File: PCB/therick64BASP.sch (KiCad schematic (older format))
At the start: 172 parts, among them J1 TYPE-C-31-M12_13, J2 AVR-ISP-6_mod, K1 KEYSW, K10 KEYSW, K11 KEYSW, K12 KEYSW, K13 KEYSW, K14 KEYSW, K15 KEYSW, K16 KEYSW, K17 KEYSW, K18 KEYSW, K19 KEYSW, K2 KEYSW, K20 KEYSW, K21 KEYSW, K22 KEYSW, K23 KEYSW, K24 KEYSW, K25 KEYSW, K26 KEYSW, K27 KEYSW, K28 KEYSW, K29 KEYSW, K3 KEYSW, K30 KEYSW, K31 KEYSW, K32 KEYSW, K33 KEYSW, K34 KEYSW, K35 KEYSW, K36 KEYSW, K37 KEYSW, K38 KEYSW, K39 KEYSW, K4 KEYSW, K40 KEYSW, K41 KEYSW, K42 KEYSW, K43 KEYSW, K44 KEYSW, K45 KEYSW, K46 KEYSW, K47 KEYSW, K48 KEYSW, K49 KEYSW, K5 KEYSW, K50 KEYSW, K51 KEYSW, K52 KEYSW, K53 KEYSW, K54 KEYSW, K55 KEYSW, K56 KEYSW, K57 KEYSW, K58 KEYSW, K59 KEYSW, K6 KEYSW, K60 KEYSW, K61 KEYSW, K62 KEYSW, K63 KEYSW, K64 KEYSW, K7 KEYSW, K8 KEYSW, K9 KEYSW, SW1 SW_PUSH, U1 ATMEGA32U4, U2 HOLE, U3 USBLC6-2SC6, U4 HOLE, U5 HOLE, U6 HOLE, U7 HOLE, Y1 16MHz

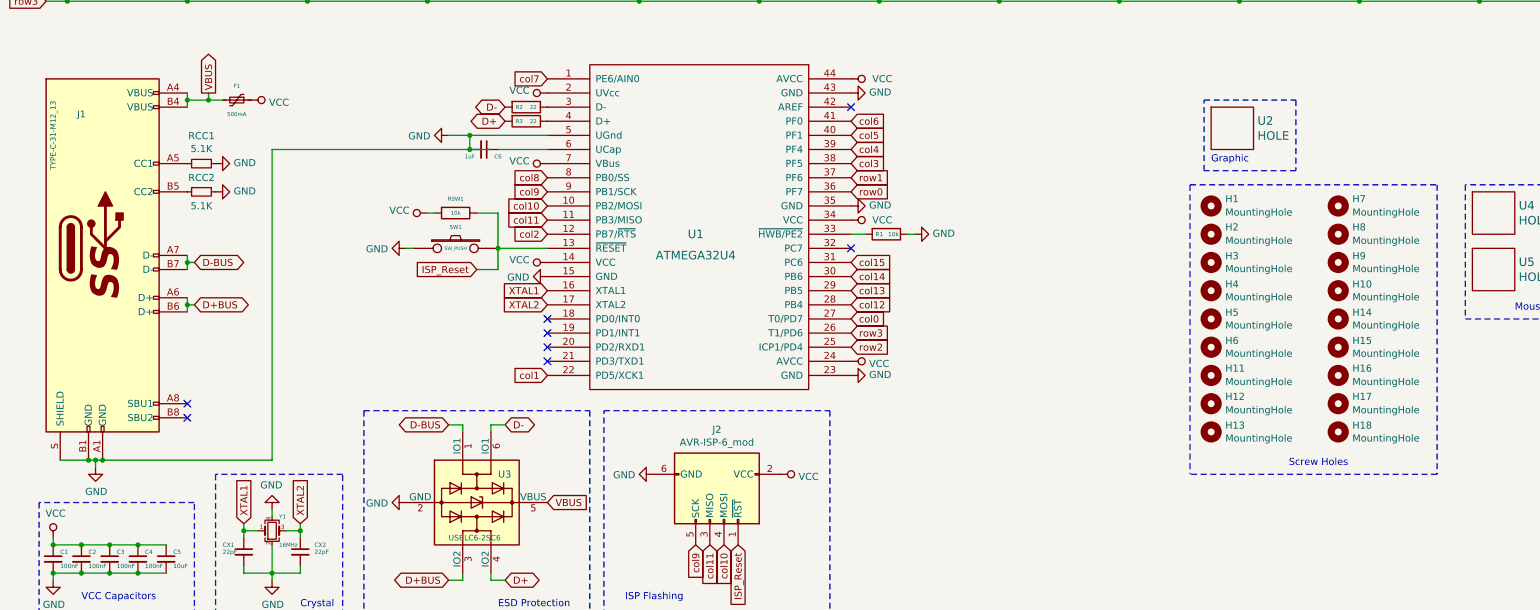
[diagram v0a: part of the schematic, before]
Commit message: Added mounting holes
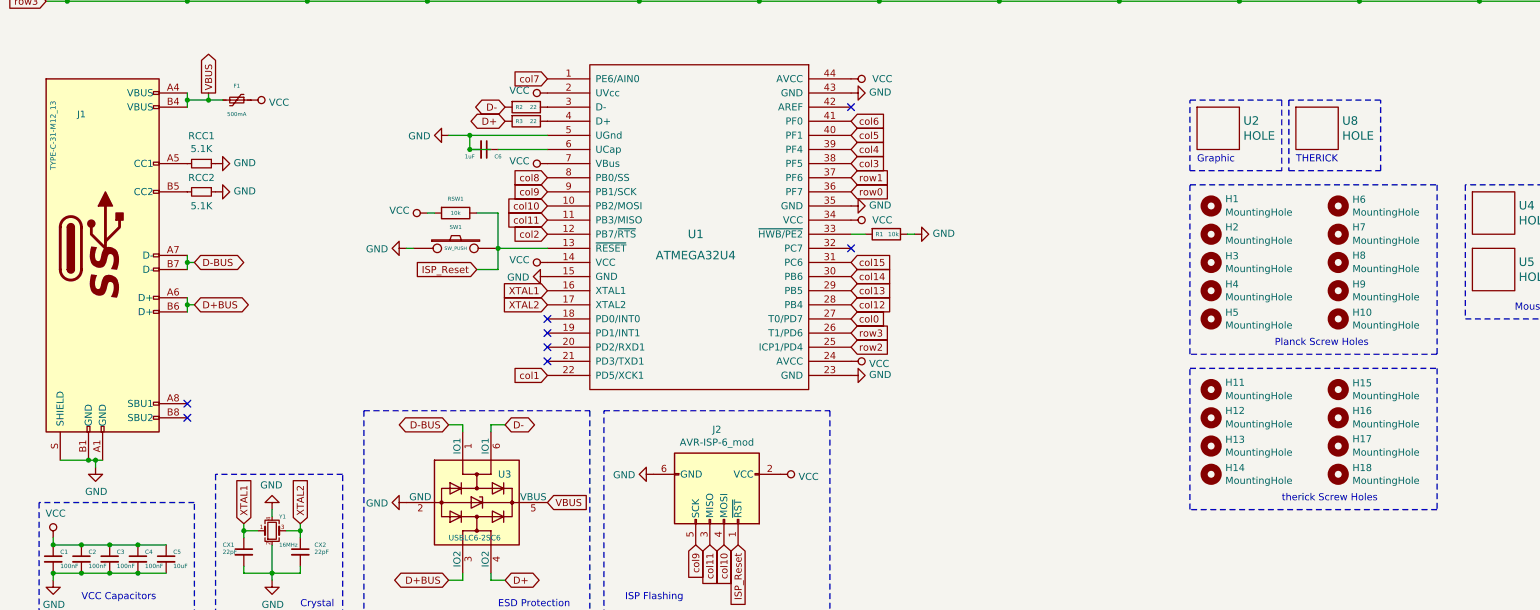
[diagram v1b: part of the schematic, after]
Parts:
- added U8: HOLE, Artwork:THERICK, symbol lets_split-cache:HOLE
- H1, H10, H11, H12, H13, H14, H15, H16, H17, H18, H2, H3, H4, H5, H6, H7, H8, H9: footprint random-keyboard-parts:plate_hole_4mm_tht -> random-keyboard-parts:Generic-Mounthole
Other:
- note added: "Planck Screw Holes"
- note added: "THERICK"
- note added: "therick Screw Holes"
- note removed: "Screw Holes"
- moved on the sheet: H10, H11, H12, H13, H14, H15, H16, H17, H18, H6, H7, H8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
